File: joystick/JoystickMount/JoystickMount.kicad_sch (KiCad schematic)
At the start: 5 parts

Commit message: update joystick mount footprint
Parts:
- H1, H2, H3, H4: footprint MountingHole:MountingHole_2.2mm_M2_DIN965 -> ErgoCai.pretty:MountingHole_2.2mm_M2_DIN965
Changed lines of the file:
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@@
 			)
 		)
-		(property "Footprint" "MountingHole:MountingHole_2.2mm_M2_DIN965"
+		(property "Footprint" "ErgoCai.pretty:MountingHole_2.2mm_M2_DIN965"
 			(at 81.28 92.71 0)
 			(effects
@@
 			)
 		)
-		(property "Footprint" "MountingHole:MountingHole_2.2mm_M2_DIN965"
+		(property "Footprint" "ErgoCai.pretty:MountingHole_2.2mm_M2_DIN965"
 			(at 102.87 100.33 0)
 			(effects
@@
 			)
 		)
-		(property "Footprint" "MountingHole:MountingHole_2.2mm_M2_DIN965"
+		(property "Footprint" "ErgoCai.pretty:MountingHole_2.2mm_M2_DIN965"
 			(at 81.28 100.33 0)
 			(effects
@@
 			)
 		)
-		(property "Footprint" "MountingHole:MountingHole_2.2mm_M2_DIN965"
+		(property "Footprint" "ErgoCai.pretty:MountingHole_2.2mm_M2_DIN965"
 			(at 102.87 92.71 0)
 			(effects

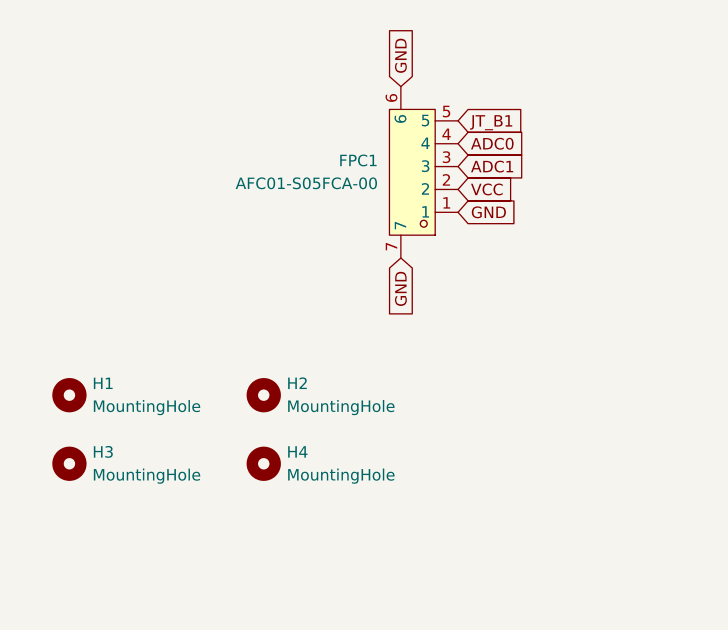
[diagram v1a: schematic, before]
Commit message: update joystick mount footprint
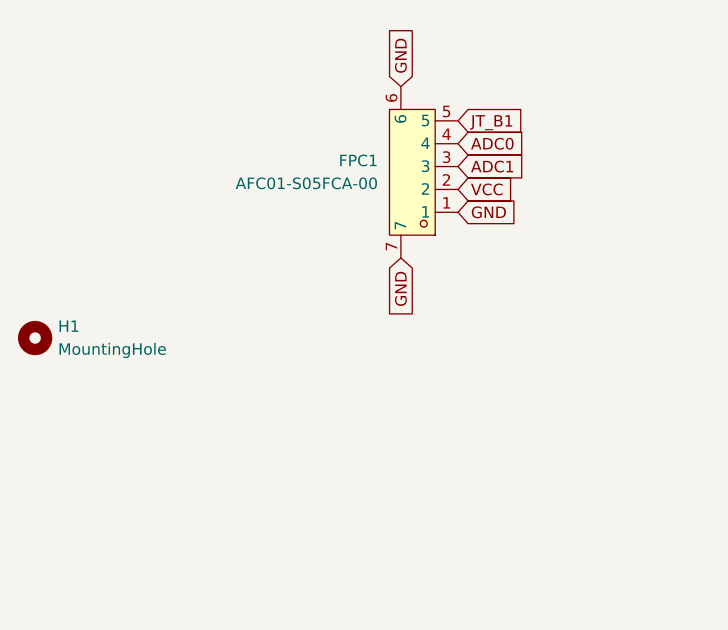
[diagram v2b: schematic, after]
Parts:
- removed H2, H3, H4: MountingHole, ErgoCai.pretty:MountingHole_2.2mm_M2_DIN965, symbol Mechanical:MountingHole
- H1: footprint ErgoCai.pretty:MountingHole_2.2mm_M2_DIN965 -> ErgoCai.pretty:Ps4JoystickMount
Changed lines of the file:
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@@
-	)
-	(symbol
-		(lib_id "Mechanical:MountingHole")
-		(at 81.28 92.71 0)
-		(unit 1)
-		(exclude_from_sim no)
-		(in_bom no)
-		(on_board yes)
-		(dnp no)
-		(fields_autoplaced yes)
-		(property "Reference" "H1"
-			(at 83.82 91.4399 0)
-			(effects
-				(font
-					(size 1.27 1.27)
-				)
-				(justify left)
-			)
-		)
-		(property "Value" "MountingHole"
-			(at 83.82 93.9799 0)
-			(effects
-				(font
-					(size 1.27 1.27)
-				)
-				(justify left)
-			)
-		)
-		(property "Footprint" "ErgoCai.pretty:MountingHole_2.2mm_M2_DIN965"
-			(at 81.28 92.71 0)
-			(effects
-				(font
-					(size 1.27 1.27)
-				)
-				(hide yes)
-			)
-		)
-		(property "Datasheet" "~"
-			(at 81.28 92.71 0)
-			(effects
-				(font
-					(size 1.27 1.27)
-				)
-				(hide yes)
-			)
-		)
-		(property "Description" "Mounting Hole without connection"
-			(at 81.28 92.71 0)
-			(effects
-				(font
-					(size 1.27 1.27)
-				)
-				(hide yes)
-			)
-		)
-		(instances
-			(project "Ps4Mount"
-				(path "/a3bb8e3e-5002-46e5-9310-dabcf88c147f"
-					(reference "H1")
-					(unit 1)
-				)
-			)
-		)
-	)
-	(symbol
-		(lib_id "Mechanical:MountingHole")
-		(at 102.87 100.33 0)
-		(unit 1)
-		(exclude_from_sim no)
-		(in_bom no)
-		(on_board yes)
-		(dnp no)
-		(fields_autoplaced yes)
-		(property "Reference" "H4"
-			(at 105.41 99.0599 0)
-			(effects
-				(font
-					(size 1.27 1.27)
-				)
-				(justify left)
-			)
-		)
-		(property "Value" "MountingHole"
-			(at 105.41 101.5999 0)
-			(effects
-				(font
-					(size 1.27 1.27)
-				)
-				(justify left)
-			)
-		)
-		(property "Footprint" "ErgoCai.pretty:MountingHole_2.2mm_M2_DIN965"
-			(at 102.87 100.33 0)
-			(effects
-				(font
-					(size 1.27 1.27)
-				)
-				(hide yes)
-			)
-		)
-		(property "Datasheet" "~"
-			(at 102.87 100.33 0)
-			(effects
-				(font
-					(size 1.27 1.27)
-				)
-				(hide yes)
-			)
-		)
-		(property "Description" "Mounting Hole without connection"
-			(at 102.87 100.33 0)
-			(effects
-				(font
-					(size 1.27 1.27)
-				)
-				(hide yes)
-			)
-		)
-		(instances
-			(project "Ps4Mount"
-				(path "/a3bb8e3e-5002-46e5-9310-dabcf88c147f"
-					(reference "H4")
-					(unit 1)
-				)
-			)
-		)
-	)
-	(symbol
-		(lib_id "Mechanical:MountingHole")
-		(at 81.28 100.33 0)
-		(unit 1)
-		(exclude_from_sim no)
-		(in_bom no)
-		(on_board yes)
-		(dnp no)
-		(fields_autoplaced yes)
-		(property "Reference" "H3"
-			(at 83.82 99.0599 0)
-			(effects
-				(font
-					(size 1.27 1.27)
-				)
-				(justify left)
-			)
-		)
-		(property "Value" "MountingHole"
-			(at 83.82 101.5999 0)
-			(effects
-				(font
-					(size 1.27 1.27)
-				)
-				(justify left)
-			)
-		)
-		(property "Footprint" "ErgoCai.pretty:MountingHole_2.2mm_M2_DIN965"
-			(at 81.28 100.33 0)
-			(effects
-				(font
-					(size 1.27 1.27)
-				)
-				(hide yes)
-			)
-		)
-		(property "Datasheet" "~"
-			(at 81.28 100.33 0)
-			(effects
-				(font
-					(size 1.27 1.27)
-				)
-				(hide yes)
-			)
-		)
-		(property "Description" "Mounting Hole without connection"
-			(at 81.28 100.33 0)
-			(effects
-				(font
-					(size 1.27 1.27)
-				)
-				(hide yes)
-			)
-		)
-		(instances
-			(project "Ps4Mount"
-				(path "/a3bb8e3e-5002-46e5-9310-dabcf88c147f"
-					(reference "H3")
-					(unit 1)
-				)
-			)
-		)
 	)
 	(symbol
@@
 	(symbol
 		(lib_id "Mechanical:MountingHole")
-		(at 102.87 92.71 0)
+		(at 77.47 86.36 0)
 		(unit 1)
 		(exclude_from_sim no)
@@
 		(dnp no)
 		(fields_autoplaced yes)
-		(property "Reference" "H2"
-			(at 105.41 91.4399 0)
+		(property "Reference" "H1"
+			(at 80.01 85.0899 0)
 			(effects
 				(font
@@
 		)
 		(property "Value" "MountingHole"
-			(at 105.41 93.9799 0)
+			(at 80.01 87.6299 0)
 			(effects
 				(font
@@
 			)
 		)
-		(property "Footprint" "ErgoCai.pretty:MountingHole_2.2mm_M2_DIN965"
-			(at 102.87 92.71 0)
+		(property "Footprint" "ErgoCai.pretty:Ps4JoystickMount"
+			(at 77.47 86.36 0)
 			(effects
 				(font
@@
 		)
 		(property "Datasheet" "~"
-			(at 102.87 92.71 0)
+			(at 77.47 86.36 0)
 			(effects
 				(font
@@
 		)
 		(property "Description" "Mounting Hole without connection"
-			(at 102.87 92.71 0)
+			(at 77.47 86.36 0)
 			(effects
 				(font
@@
 		)
 		(instances
-			(project "Ps4Mount"
+			(project ""
 				(path "/a3bb8e3e-5002-46e5-9310-dabcf88c147f"
-					(reference "H2")
+					(reference "H1")
 					(unit 1)
 				)

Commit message: update joystick mount connector to JST ZH
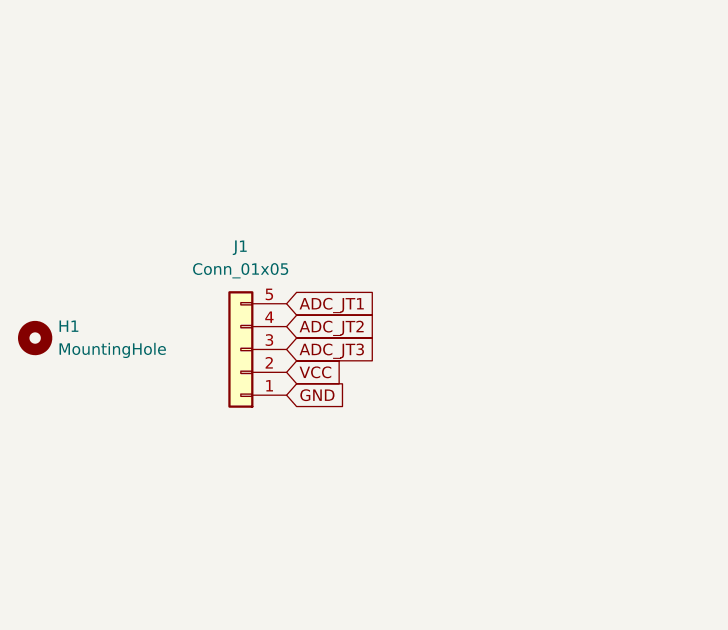
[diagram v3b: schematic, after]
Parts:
- removed FPC1: AFC01-S05FCA-00, ErgoCai.pretty:FPC-SMD_AFC01-S05FCA-00, symbol ErgoCai:AFC01-S05FCA-00
- added J1: Conn_01x05, ErgoCai.pretty:CONN-TH_S5B-ZR-LF-SN, symbol Connector_Generic:Conn_01x05
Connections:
- net GND: now also J1.1 (Pin_1)
- net VCC: now also J1.2 (Pin_2)
- new net ADC_JT1: J1.5 (Pin_5)
- new net ADC_JT2: J1.4 (Pin_4)
- new net ADC_JT3: J1.3 (Pin_3)
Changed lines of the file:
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@@
 	(generator_version "9.0")
 	(paper "A4")
-	(global_label "ADC1"
+	(global_label "VCC"
 		(shape input)
-		(at 124.46 67.31 0)
+		(at 105.41 90.17 0)
 		(fields_autoplaced yes)
 		(effects
@@
 		)
 		(property "Intersheetrefs" "${INTERSHEET_REFS}"
-			(at 132.2833 67.31 0)
+			(at 112.0238 90.17 0)
 			(effects
 				(font
@@
 	(global_label "GND"
 		(shape input)
-		(at 124.46 72.39 0)
+		(at 105.41 92.71 0)
 		(fields_autoplaced yes)
 		(effects
@@
 		)
 		(property "Intersheetrefs" "${INTERSHEET_REFS}"
-			(at 131.3157 72.39 0)
+			(at 112.2657 92.71 0)
 			(effects
 				(font
@@
 		)
 	)
-	(global_label "JT_B1"
+	(global_label "ADC_JT1"
 		(shape input)
-		(at 124.46 62.23 0)
+		(at 105.41 82.55 0)
 		(fields_autoplaced yes)
 		(effects
@@
 		)
 		(property "Intersheetrefs" "${INTERSHEET_REFS}"
-			(at 132.8275 62.23 0)
+			(at 116.1361 82.55 0)
 			(effects
 				(font
@@
 		)
 	)
-	(global_label "GND"
+	(global_label "ADC_JT2"
 		(shape input)
-		(at 118.11 77.47 270)
-		(fields_autoplaced yes)
-		(effects
-			(font
-				(size 1.27 1.27)
-			)
-			(justify right)
-		)
-		(property "Intersheetrefs" "${INTERSHEET_REFS}"
-			(at 118.11 84.3257 90)
-			(effects
-				(font
-					(size 1.27 1.27)
-				)
-				(justify right)
-				(hide yes)
-			)
-		)
-	)
-	(global_label "VCC"
-		(shape input)
-		(at 124.46 69.85 0)
+		(at 105.41 85.09 0)
 		(fields_autoplaced yes)
 		(effects
@@
 		)
 		(property "Intersheetrefs" "${INTERSHEET_REFS}"
-			(at 131.0738 69.85 0)
+			(at 116.1361 85.09 0)
 			(effects
 				(font
@@
 		)
 	)
-	(global_label "GND"
+	(global_label "ADC_JT3"
 		(shape input)
-		(at 118.11 58.42 90)
+		(at 105.41 87.63 0)
 		(fields_autoplaced yes)
 		(effects
@@
 		)
 		(property "Intersheetrefs" "${INTERSHEET_REFS}"
-			(at 118.11 51.5643 90)
-			(effects
-				(font
-					(size 1.27 1.27)
-				)
-				(justify left)
-				(hide yes)
-			)
-		)
-	)
-	(global_label "ADC0"
-		(shape input)
-		(at 124.46 64.77 0)
-		(fields_autoplaced yes)
-		(effects
-			(font
-				(size 1.27 1.27)
-			)
-			(justify left)
-		)
-		(property "Intersheetrefs" "${INTERSHEET_REFS}"
-			(at 132.2833 64.77 0)
+			(at 116.1361 87.63 0)
 			(effects
 				(font
@@
 	)
 	(symbol
-		(lib_id "ErgoCai:AFC01-S05FCA-00")
-		(at 120.65 67.31 180)
+		(lib_id "Connector_Generic:Conn_01x05")
+		(at 100.33 87.63 180)
 		(unit 1)
 		(exclude_from_sim no)
@@
 		(dnp no)
 		(fields_autoplaced yes)
-		(property "Reference" "FPC1"
-			(at 115.57 66.6749 0)
+		(property "Reference" "J1"
+			(at 100.33 76.2 0)
 			(effects
 				(font
 					(size 1.27 1.27)
 				)
-				(justify left)
 			)
 		)
-		(property "Value" "AFC01-S05FCA-00"
-			(at 115.57 69.2149 0)
+		(property "Value" "Conn_01x05"
+			(at 100.33 78.74 0)
 			(effects
 				(font
 					(size 1.27 1.27)
 				)
-				(justify left)
 			)
 		)
-		(property "Footprint" "ErgoCai.pretty:FPC-SMD_AFC01-S05FCA-00"
-			(at 120.65 50.8 0)
+		(property "Footprint" "ErgoCai.pretty:CONN-TH_S5B-ZR-LF-SN"
+			(at 100.33 87.63 0)
 			(effects
 				(font
@@
 			)
 		)
-		(property "Datasheet" "https://lcsc.com/product-detail/FFC-FPC-Connectors_JUSHUO-AFC01-S05FCA-00_C262654.html"
-			(at 120.65 48.26 0)
+		(property "Datasheet" "~"
+			(at 100.33 87.63 0)
 			(effects
 				(font
@@
 			)
 		)
-		(property "Description" ""
-			(at 120.65 67.31 0)
+		(property "Description" "Generic connector, single row, 01x05, script generated (kicad-library-utils/schlib/autogen/connector/)"
+			(at 100.33 87.63 0)
 			(effects
 				(font
@@
 			)
 		)
-		(property "LCSC Part" "C262654"
-			(at 120.65 45.72 0)
-			(effects
-				(font
-					(size 1.27 1.27)
-				)
-				(hide yes)
-			)
+		(pin "4"
 		)
-		(pin "1"
+		(pin "5"
 		)
 		(pin "2"
@@
 		(pin "3"
 		)
-		(pin "4"
-		)
-		(pin "6"
-		)
-		(pin "5"
-		)
-		(pin "7"
+		(pin "1"
 		)
 		(instances
-			(project "Ps4Mount"
+			(project "JoystickMount"
 				(path "/a3bb8e3e-5002-46e5-9310-dabcf88c147f"
-					(reference "FPC1")
+					(reference "J1")
 					(unit 1)
 				)

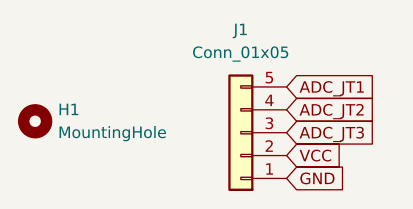
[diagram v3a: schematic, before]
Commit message: update to 3.3V tag
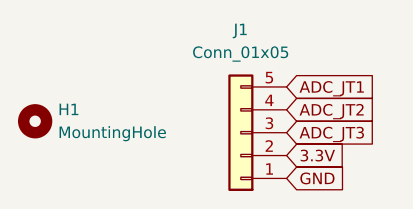
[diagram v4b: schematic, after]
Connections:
- net VCC renamed 3.3V
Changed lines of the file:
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@@
 	(generator_version "9.0")
 	(paper "A4")
-	(global_label "VCC"
+	(global_label "3.3V"
 		(shape input)
 		(at 105.41 90.17 0)
@@
 		)
 		(property "Intersheetrefs" "${INTERSHEET_REFS}"
-			(at 112.0238 90.17 0)
+			(at 112.5076 90.17 0)
 			(effects
 				(font

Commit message: update reference in joystick and e-paper
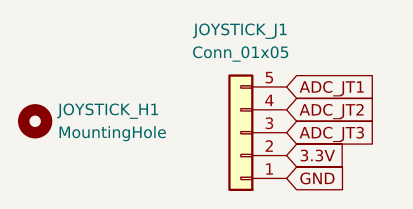
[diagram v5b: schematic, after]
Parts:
- renumbered H1 to JOYSTICK_H1, J1 to JOYSTICK_J1
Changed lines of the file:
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@@
 		(dnp no)
 		(fields_autoplaced yes)
-		(property "Reference" "J1"
+		(property "Reference" "JOYSTICK_J1"
 			(at 100.33 76.2 0)
 			(effects
@@
 			(project "JoystickMount"
 				(path "/a3bb8e3e-5002-46e5-9310-dabcf88c147f"
-					(reference "J1")
+					(reference "JOYSTICK_J1")
 					(unit 1)
 				)
@@
 		(dnp no)
 		(fields_autoplaced yes)
-		(property "Reference" "H1"
+		(property "Reference" "JOYSTICK_H1"
 			(at 80.01 85.0899 0)
 			(effects
@@
 			(project ""
 				(path "/a3bb8e3e-5002-46e5-9310-dabcf88c147f"
-					(reference "H1")
+					(reference "JOYSTICK_H1")
 					(unit 1)
 				)

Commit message: update joystick mount
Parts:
- JOYSTICK_J1: footprint ErgoCai.pretty:CONN-TH_S5B-ZR-LF-SN -> ErgoCai.pretty:FPC-SMD_AFC01-S05FCA-00
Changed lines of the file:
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@@
 			)
 		)
-		(property "Footprint" "ErgoCai.pretty:CONN-TH_S5B-ZR-LF-SN"
+		(property "Footprint" "ErgoCai.pretty:FPC-SMD_AFC01-S05FCA-00"
 			(at 100.33 87.63 0)
 			(effects
